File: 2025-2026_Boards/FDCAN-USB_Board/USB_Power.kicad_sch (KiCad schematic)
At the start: 7 parts, among them J1 USB4110GFA, U1 AMS1117-3.3, U2 USBLC6-2SC6

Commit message: microcontroller pin update
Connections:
- net USB_N renamed USB_DM
- net USB_P renamed USB_DP
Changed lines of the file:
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@@
 		)
 	)
-	(global_label "USB_P"
+	(global_label "USB_DP"
 		(shape input)
 		(at 149.86 107.95 180)
@@
 		)
 		(property "Intersheetrefs" "${INTERSHEET_REFS}"
-			(at 140.8272 107.95 0)
+			(at 139.5572 107.95 0)
 			(effects
 				(font
@@
 		)
 	)
-	(global_label "USB_N"
+	(global_label "USB_DM"
 		(shape input)
 		(at 149.86 82.55 180)
@@
 		)
 		(property "Intersheetrefs" "${INTERSHEET_REFS}"
-			(at 140.7667 82.55 0)
+			(at 139.3758 82.55 0)
 			(effects
 				(font

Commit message: grouped components
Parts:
- added C16: 100n, Capacitor_SMD:C_0402_1005Metric, symbol Device:C
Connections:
- net 5V: now also C16.1
- net GND: now also C16.2
- net USB+: now also U2.1; no longer U2.4
- net USB-: now also U2.3; no longer U2.6
- net USB_DM: now also U2.4; no longer U2.1
- net USB_DP: now also U2.6; no longer U2.3

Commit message: Layout finished
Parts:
- removed J1: USB4110GFA, Cornell_Mars_Rover:GCT_USB4110GFA, symbol Cornell_Mars_Rover:USB4110GFA
- added J7: USB4110-GF-A, Cornell_Mars_Rover:USB4110-GF-A_GCT, symbol Cornell_Mars_Rover:USB4110-GF-A
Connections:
- net 5V: now also J7.A4-B9 (VBUS), J7.A9-B4 (VBUS)
- net GND: now also R1.1, R2.1, J7.A1-B12 (GND), J7.A12-B1 (GND); no longer R1.2, R2.2
- net USB+: now also J7.A6 (DP1), J7.B6 (DP2)
- net USB-: now also J7.A7 (DN1), J7.B7 (DN2)
- net USB_DM renamed USB_N
- net USB_DP renamed USB_P
- new net: J7.A5 (CC1), R2.2
- new net: J7.B5 (CC2), R1.2
- no-connect marks 6 -> 2
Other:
- moved on the sheet: R1, R2

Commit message: Final Design Reupload
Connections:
- net GND: now also R2.2; no longer R2.1
- net at J7.A5 (CC1): now also R2.1; no longer R2.2
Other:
- moved on the sheet: C1, C16, C2, J7, R1, U1, U2

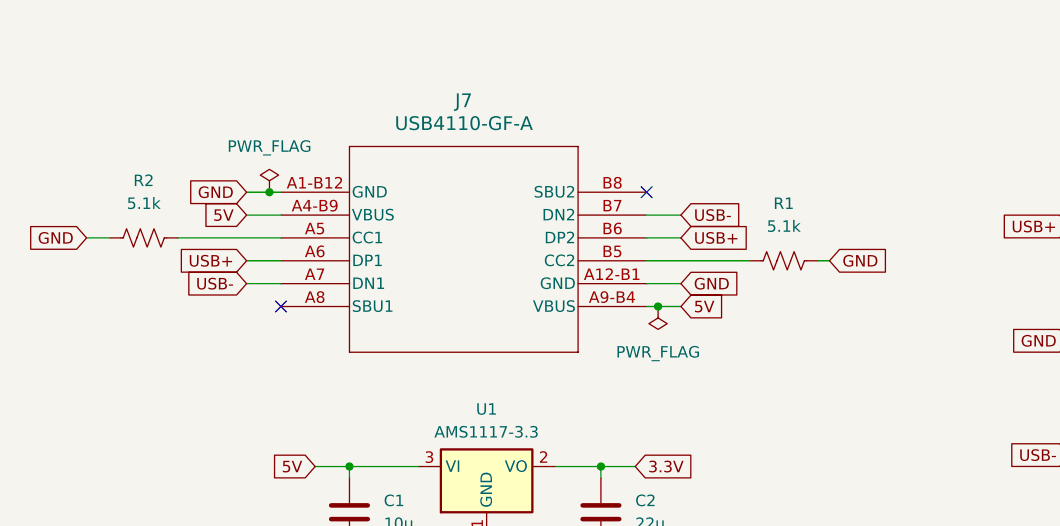
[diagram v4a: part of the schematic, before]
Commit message: USB swap and updated BOM
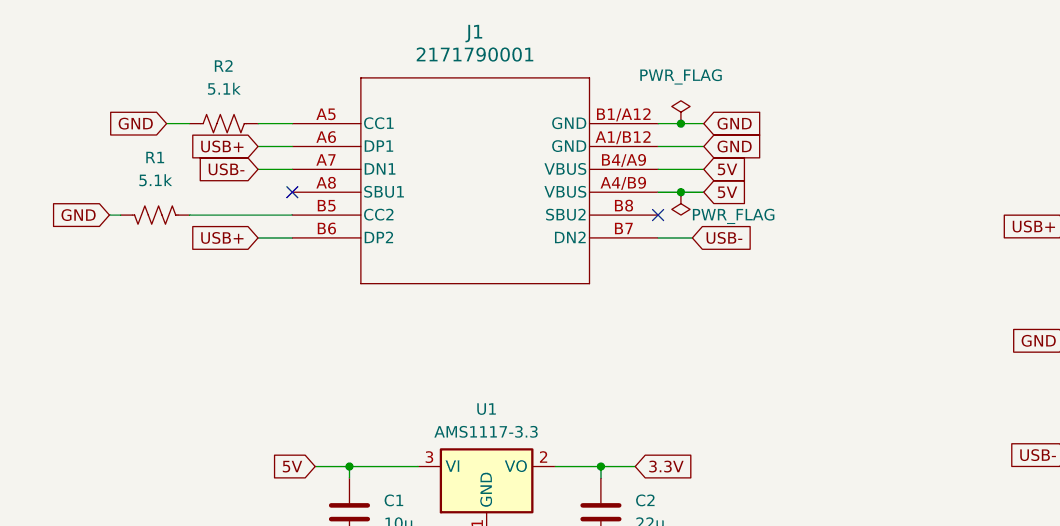
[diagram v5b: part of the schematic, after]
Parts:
- removed J7: USB4110-GF-A, Cornell_Mars_Rover:USB4110-GF-A_GCT, symbol Cornell_Mars_Rover:USB4110-GF-A
- added J1: 2171790001, Cornell_Mars_Rover:2171790001_MOL, symbol Cornell_Mars_Rover:2171790001
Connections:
- net 5V: now also J1.A4/B9 (VBUS), J1.B4/A9 (VBUS)
- net GND: now also J1.A1/B12 (GND), J1.B1/A12 (GND)
- net USB+: now also J1.A6 (DP1), J1.B6 (DP2)
- net USB-: now also J1.A7 (DN1), J1.B7 (DN2)
- net at R1.2: now also J1.B5 (CC2)
- net at R2.1: now also J1.A5 (CC1)
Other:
- moved on the sheet: R1, R2
